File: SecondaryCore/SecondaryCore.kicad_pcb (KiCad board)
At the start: 2 copper layers, 88.9 x 35.6 mm, 7 parts, among them J1 Screw_Terminal_01x02, J2 Screw_Terminal_01x02

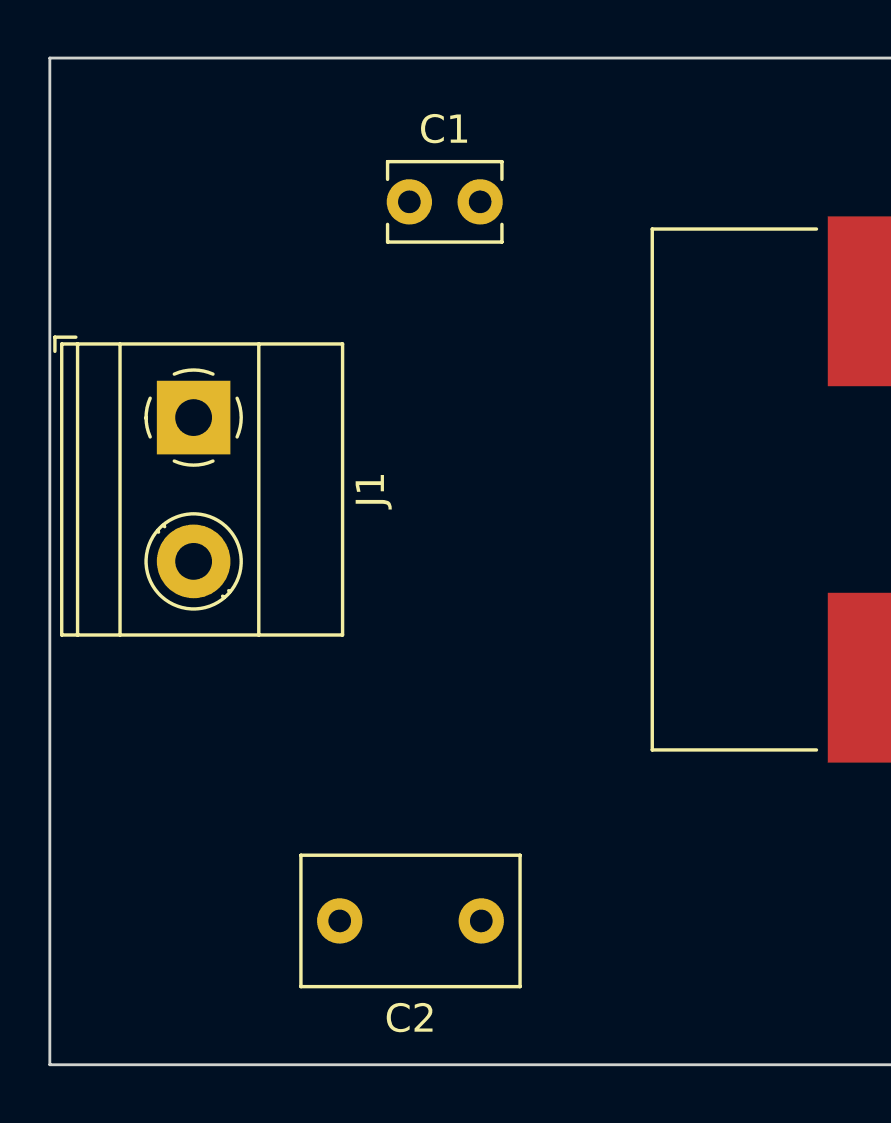
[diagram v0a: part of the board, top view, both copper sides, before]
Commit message: Change Cap footpackage p 10mm
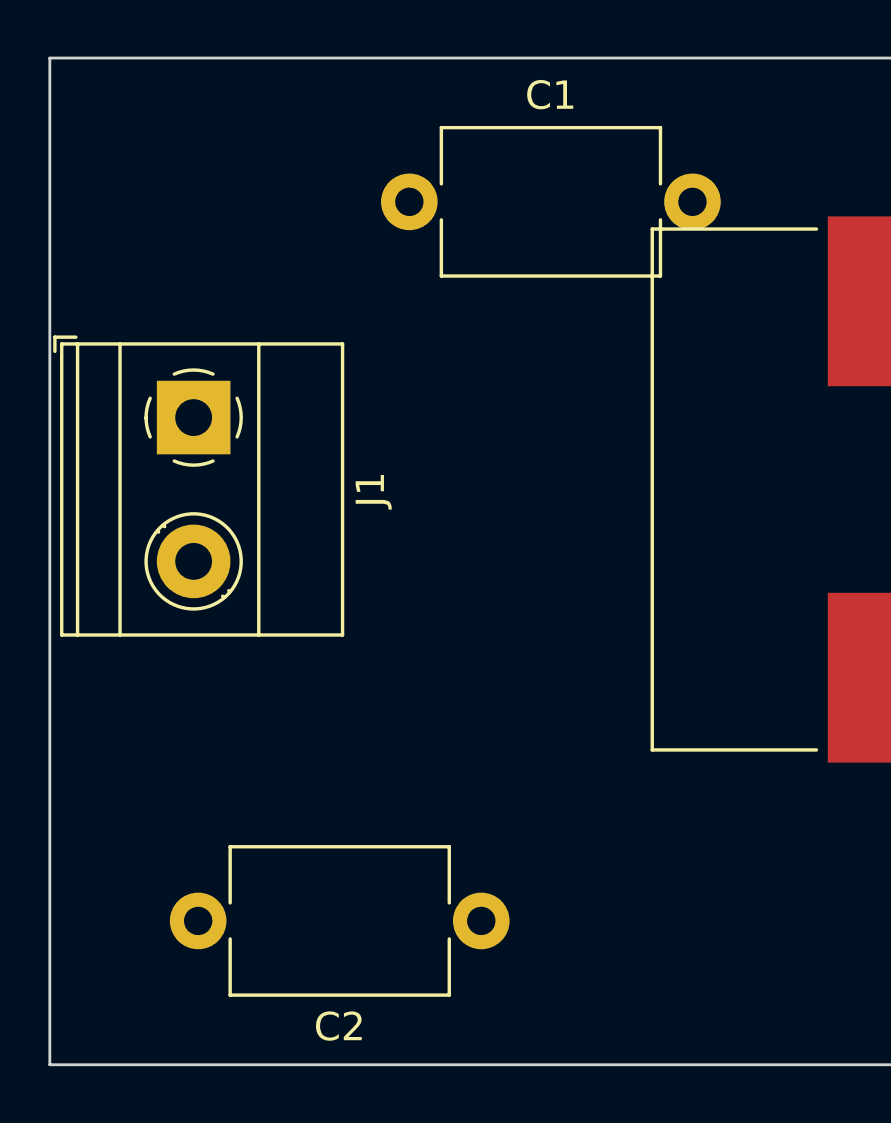
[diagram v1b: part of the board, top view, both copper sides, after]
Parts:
- C1: footprint Capacitor_THT:C_Disc_D3.8mm_W2.6mm_P2.50mm -> Capacitor_THT:C_Disc_D7.5mm_W5.0mm_P10.00mm
- C2: footprint Capacitor_THT:C_Disc_D7.5mm_W4.4mm_P5.00mm -> Capacitor_THT:C_Disc_D7.5mm_W5.0mm_P10.00mm
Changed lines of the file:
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@@
     )
   )
-  (footprint "Capacitor_THT:C_Disc_D7.5mm_W4.4mm_P5.00mm" (layer "F.Cu")
+  (footprint "Capacitor_THT:C_Disc_D7.5mm_W5.0mm_P10.00mm" (layer "F.Cu")
     (at 109.22 106.68 180)
-    (descr "C, Disc series, Radial, pin pitch=5.00mm, , diameter*width=7.5*4.4mm^2, Capacitor")
-    (tags "C Disc series Radial pin pitch 5.00mm  diameter 7.5mm width 4.4mm Capacitor")
+    (descr "C, Disc series, Radial, pin pitch=10.00mm, , diameter*width=7.5*5.0mm^2, Capacitor, http://www.vishay.com/docs/28535/vy2series.pdf")
+    (tags "C Disc series Radial pin pitch 10.00mm  diameter 7.5mm width 5.0mm Capacitor")
     (property "Sheetfile" "SecondaryCore.kicad_sch")
     (property "Sheetname" "")
     (attr through_hole)
-    (fp_text reference "C2" (at 2.5 -3.45) (layer "F.SilkS")
+    (fp_text reference "C2" (at 5 -3.75 180) (layer "F.SilkS")
       (effects (font (size 1 1) (thickness 0.15)))
     )
-    (fp_text value "330pF" (at 2.5 3.45) (layer "F.Fab")
+    (fp_text value "330pF" (at 5 3.75 180) (layer "F.Fab")
       (effects (font (size 1 1) (thickness 0.15)))
     )
-    (fp_text user "${REFERENCE}" (at 2.5 0) (layer "F.Fab")
+    (fp_text user "${REFERENCE}" (at 5 0 180) (layer "F.Fab")
       (effects (font (size 1 1) (thickness 0.15)))
     )
-    (fp_line (start -1.37 2.321) (end 6.37 2.321) (layer "F.SilkS") (width 0.12))
-    (fp_line (start 6.37 -2.321) (end 6.37 2.321) (layer "F.SilkS") (width 0.12))
-    (fp_line (start -1.37 -2.321) (end 6.37 -2.321) (layer "F.SilkS") (width 0.12))
-    (fp_line (start -1.37 -2.321) (end -1.37 2.321) (layer "F.SilkS") (width 0.12))
-    (fp_line (start -1.5 2.45) (end 6.5 2.45) (layer "F.CrtYd") (width 0.05))
-    (fp_line (start -1.5 -2.45) (end -1.5 2.45) (layer "F.CrtYd") (width 0.05))
-    (fp_line (start 6.5 2.45) (end 6.5 -2.45) (layer "F.CrtYd") (width 0.05))
-    (fp_line (start 6.5 -2.45) (end -1.5 -2.45) (layer "F.CrtYd") (width 0.05))
-    (fp_line (start 6.25 2.2) (end 6.25 -2.2) (layer "F.Fab") (width 0.1))
-    (fp_line (start 6.25 -2.2) (end -1.25 -2.2) (layer "F.Fab") (width 0.1))
-    (fp_line (start -1.25 2.2) (end 6.25 2.2) (layer "F.Fab") (width 0.1))
-    (fp_line (start -1.25 -2.2) (end -1.25 2.2) (layer "F.Fab") (width 0.1))
-    (pad "1" thru_hole circle (at 0 0 180) (size 1.6 1.6) (drill 0.8) (layers *.Cu *.Mask)
+    (fp_line (start 1.13 -2.62) (end 8.87 -2.62) (layer "F.SilkS") (width 0.12))
+    (fp_line (start 1.13 -2.62) (end 1.13 -0.636) (layer "F.SilkS") (width 0.12))
+    (fp_line (start 1.13 0.636) (end 1.13 2.62) (layer "F.SilkS") (width 0.12))
+    (fp_line (start 8.87 -2.62) (end 8.87 -0.636) (layer "F.SilkS") (width 0.12))
+    (fp_line (start 8.87 0.636) (end 8.87 2.62) (layer "F.SilkS") (width 0.12))
+    (fp_line (start 1.13 2.62) (end 8.87 2.62) (layer "F.SilkS") (width 0.12))
+    (fp_line (start 11.25 2.75) (end 11.25 -2.75) (layer "F.CrtYd") (width 0.05))
+    (fp_line (start 11.25 -2.75) (end -1.25 -2.75) (layer "F.CrtYd") (width 0.05))
+    (fp_line (start -1.25 2.75) (end 11.25 2.75) (layer "F.CrtYd") (width 0.05))
+    (fp_line (start -1.25 -2.75) (end -1.25 2.75) (layer "F.CrtYd") (width 0.05))
+    (fp_line (start 8.75 2.5) (end 8.75 -2.5) (layer "F.Fab") (width 0.1))
+    (fp_line (start 1.25 2.5) (end 8.75 2.5) (layer "F.Fab") (width 0.1))
+    (fp_line (start 8.75 -2.5) (end 1.25 -2.5) (layer "F.Fab") (width 0.1))
+    (fp_line (start 1.25 -2.5) (end 1.25 2.5) (layer "F.Fab") (width 0.1))
+    (pad "1" thru_hole circle (at 0 0 180) (size 2 2) (drill 1) (layers *.Cu *.Mask)
       (net 2 "Net-(C1-Pad2)") (pintype "passive"))
-    (pad "2" thru_hole circle (at 5 0 180) (size 1.6 1.6) (drill 0.8) (layers *.Cu *.Mask)
+    (pad "2" thru_hole circle (at 10 0 180) (size 2 2) (drill 1) (layers *.Cu *.Mask)
       (net 3 "Net-(C2-Pad2)") (pintype "passive"))
-    (model "${KICAD6_3DMODEL_DIR}/Capacitor_THT.3dshapes/C_Disc_D7.5mm_W4.4mm_P5.00mm.wrl"
+    (model "${KICAD6_3DMODEL_DIR}/Capacitor_THT.3dshapes/C_Disc_D7.5mm_W5.0mm_P10.00mm.wrl"
       (offset (xyz 0 0 0))
       (scale (xyz 1 1 1))
@@
     )
   )
-  (footprint "Capacitor_THT:C_Disc_D3.8mm_W2.6mm_P2.50mm" (layer "F.Cu")
+  (footprint "Capacitor_THT:C_Disc_D7.5mm_W5.0mm_P10.00mm" (layer "F.Cu")
     (at 106.68 81.28)
-    (descr "C, Disc series, Radial, pin pitch=2.50mm, , diameter*width=3.8*2.6mm^2, Capacitor, http://www.vishay.com/docs/45233/krseries.pdf")
-    (tags "C Disc series Radial pin pitch 2.50mm  diameter 3.8mm width 2.6mm Capacitor")
+    (descr "C, Disc series, Radial, pin pitch=10.00mm, , diameter*width=7.5*5.0mm^2, Capacitor, http://www.vishay.com/docs/28535/vy2series.pdf")
+    (tags "C Disc series Radial pin pitch 10.00mm  diameter 7.5mm width 5.0mm Capacitor")
     (property "Sheetfile" "SecondaryCore.kicad_sch")
     (property "Sheetname" "")
     (attr through_hole)
-    (fp_text reference "C1" (at 1.25 -2.55) (layer "F.SilkS")
+    (fp_text reference "C1" (at 5 -3.75) (layer "F.SilkS")
       (effects (font (size 1 1) (thickness 0.15)))
     )
-    (fp_text value "270pF" (at 1.25 2.55) (layer "F.Fab")
+    (fp_text value "270pF" (at 5 3.75) (layer "F.Fab")
       (effects (font (size 1 1) (thickness 0.15)))
     )
-    (fp_text user "${REFERENCE}" (at 1.25 0) (layer "F.Fab")
-      (effects (font (size 0.76 0.76) (thickness 0.114)))
+    (fp_text user "${REFERENCE}" (at 5 0) (layer "F.Fab")
+      (effects (font (size 1 1) (thickness 0.15)))
     )
-    (fp_line (start -0.77 0.795) (end -0.77 1.42) (layer "F.SilkS") (width 0.12))
-    (fp_line (start 3.27 0.795) (end 3.27 1.42) (layer "F.SilkS") (width 0.12))
-    (fp_line (start -0.77 -1.42) (end -0.77 -0.795) (layer "F.SilkS") (width 0.12))
-    (fp_line (start -0.77 1.42) (end 3.27 1.42) (layer "F.SilkS") (width 0.12))
-    (fp_line (start -0.77 -1.42) (end 3.27 -1.42) (layer "F.SilkS") (width 0.12))
-    (fp_line (start 3.27 -1.42) (end 3.27 -0.795) (layer "F.SilkS") (width 0.12))
-    (fp_line (start 3.55 1.55) (end 3.55 -1.55) (layer "F.CrtYd") (width 0.05))
-    (fp_line (start 3.55 -1.55) (end -1.05 -1.55) (layer "F.CrtYd") (width 0.05))
-    (fp_line (start -1.05 1.55) (end 3.55 1.55) (layer "F.CrtYd") (width 0.05))
-    (fp_line (start -1.05 -1.55) (end -1.05 1.55) (layer "F.CrtYd") (width 0.05))
-    (fp_line (start -0.65 1.3) (end 3.15 1.3) (layer "F.Fab") (width 0.1))
-    (fp_line (start 3.15 1.3) (end 3.15 -1.3) (layer "F.Fab") (width 0.1))
-    (fp_line (start -0.65 -1.3) (end -0.65 1.3) (layer "F.Fab") (width 0.1))
-    (fp_line (start 3.15 -1.3) (end -0.65 -1.3) (layer "F.Fab") (width 0.1))
-    (pad "1" thru_hole circle (at 0 0) (size 1.6 1.6) (drill 0.8) (layers *.Cu *.Mask)
+    (fp_line (start 1.13 -2.62) (end 1.13 -0.636) (layer "F.SilkS") (width 0.12))
+    (fp_line (start 1.13 2.62) (end 8.87 2.62) (layer "F.SilkS") (width 0.12))
+    (fp_line (start 8.87 -2.62) (end 8.87 -0.636) (layer "F.SilkS") (width 0.12))
+    (fp_line (start 1.13 0.636) (end 1.13 2.62) (layer "F.SilkS") (width 0.12))
+    (fp_line (start 1.13 -2.62) (end 8.87 -2.62) (layer "F.SilkS") (width 0.12))
+    (fp_line (start 8.87 0.636) (end 8.87 2.62) (layer "F.SilkS") (width 0.12))
+    (fp_line (start -1.25 -2.75) (end -1.25 2.75) (layer "F.CrtYd") (width 0.05))
+    (fp_line (start -1.25 2.75) (end 11.25 2.75) (layer "F.CrtYd") (width 0.05))
+    (fp_line (start 11.25 -2.75) (end -1.25 -2.75) (layer "F.CrtYd") (width 0.05))
+    (fp_line (start 11.25 2.75) (end 11.25 -2.75) (layer "F.CrtYd") (width 0.05))
+    (fp_line (start 1.25 2.5) (end 8.75 2.5) (layer "F.Fab") (width 0.1))
+    (fp_line (start 1.25 -2.5) (end 1.25 2.5) (layer "F.Fab") (width 0.1))
+    (fp_line (start 8.75 -2.5) (end 1.25 -2.5) (layer "F.Fab") (width 0.1))
+    (fp_line (start 8.75 2.5) (end 8.75 -2.5) (layer "F.Fab") (width 0.1))
+    (pad "1" thru_hole circle (at 0 0) (size 2 2) (drill 1) (layers *.Cu *.Mask)
       (net 1 "Net-(C1-Pad1)") (pintype "passive"))
-    (pad "2" thru_hole circle (at 2.5 0) (size 1.6 1.6) (drill 0.8) (layers *.Cu *.Mask)
+    (pad "2" thru_hole circle (at 10 0) (size 2 2) (drill 1) (layers *.Cu *.Mask)
       (net 2 "Net-(C1-Pad2)") (pintype "passive"))
-    (model "${KICAD6_3DMODEL_DIR}/Capacitor_THT.3dshapes/C_Disc_D3.8mm_W2.6mm_P2.50mm.wrl"
+    (model "${KICAD6_3DMODEL_DIR}/Capacitor_THT.3dshapes/C_Disc_D7.5mm_W5.0mm_P10.00mm.wrl"
       (offset (xyz 0 0 0))
       (scale (xyz 1 1 1))

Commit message: latest route pcb
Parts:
- C3: footprint TerminalBlock_Phoenix:TerminalBlock_Phoenix_MPT-0,5-2-2.54_1x02_P2.54mm_Horizontal -> Capacitor_THT:CP_Radial_D18.0mm_P7.50mm
- moved C2 30.6 mm to (139.8, 106.7), turned to 0 degrees
- moved C1 25.5 mm to (104.2, 106.7)
- moved C3 21.6 mm to (177.8, 86.4)
- moved J2 9.33 mm to (183.2, 101.6)
- moved D1 6.97 mm to (146.9, 91.4), turned to 45 degrees
- moved L1 2.54 mm to (127.0, 91.4), turned to 90 degrees
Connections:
- D1 pad 1: Net-(C3-Pad1) -> Net-(C3-Pad2)
- D1 pad 3: Net-(C3-Pad2) -> Net-(C3-Pad1)
- J2 pad 1: Net-(C3-Pad1) -> Net-(C3-Pad2)
- J2 pad 2: Net-(C3-Pad2) -> Net-(C3-Pad1)
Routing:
- net Net-(C3-Pad2): track 0.00 -> 76.6 mm
- net Net-(C2-Pad2): track 0.00 -> 68.0 mm
- net Net-(C3-Pad1): track 0.00 -> 42.0 mm
- net Net-(C1-Pad2): track 0.00 -> 35.2 mm
- net Net-(D1-Pad4): track 0.00 -> 27.6 mm
- net Net-(C1-Pad1): track 0.00 -> 14.8 mm
- added copper zone on B.Cu, net (none)
- added copper zone on F.Cu, net (none)
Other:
- board size 88.9 x 35.6 mm -> 94.6 x 39.4 mm
- board text added: "COIL"
- board text added: "OUTPUT"
